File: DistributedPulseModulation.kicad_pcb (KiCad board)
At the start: 2 copper layers, 95.9 x 90.2 mm, 41 parts, among them J1 Conn_02x12_Odd_Even, J2 Conn_02x05_Odd_Even, U1 74LS251, U2 74LVC2G74, U25 74LS85, U28 74LS85, U3 ADG333A, U31 74LS85, U4 MCP23017_SP, U5 ADG333A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

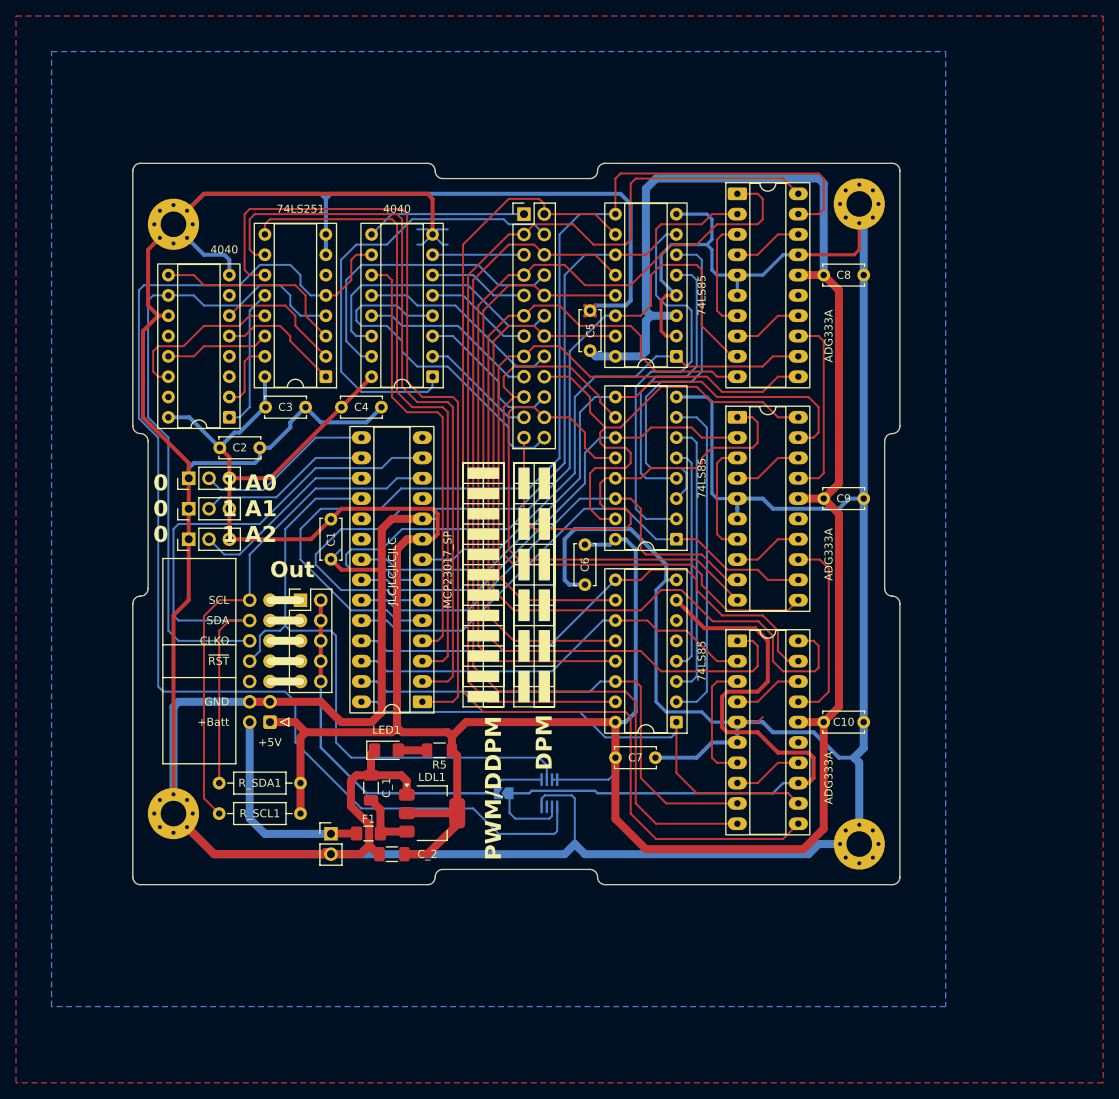
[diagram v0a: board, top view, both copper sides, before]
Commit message: RETROFIT : connecteur perso PCIe_CAN pour compatibilité avec le CANduino128 comme microcontôleur maitre
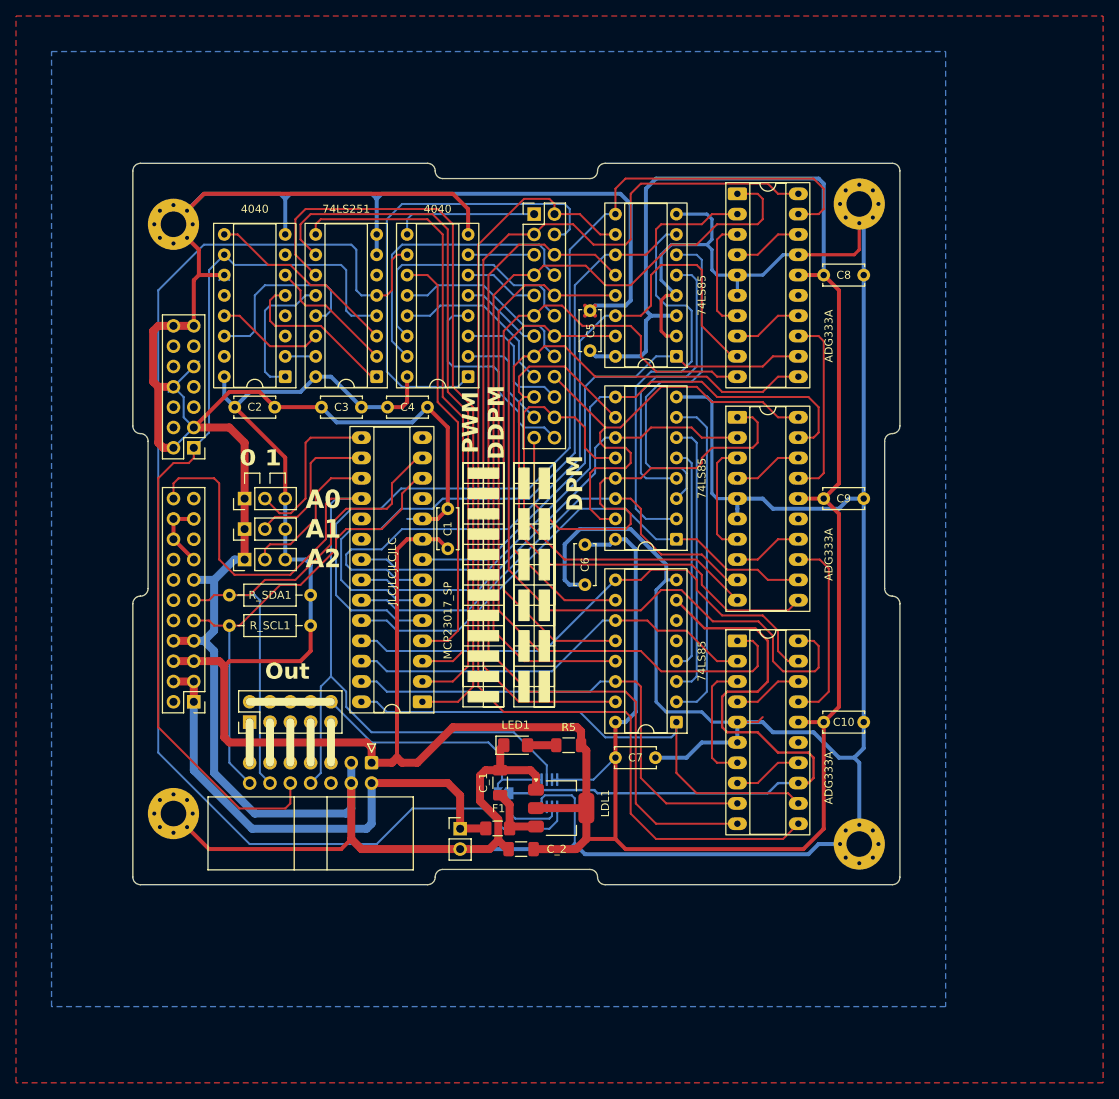
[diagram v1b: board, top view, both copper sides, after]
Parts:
- added PCIe_CAN_1: Conn_02x07_Odd_Even, Connector_PinHeader_2.54mm:PinHeader_2x07_P2.54mm_Vertical, F.Cu at (48.9, 80.0)
- added PCIe_SPI_1: Conn_02x11_Odd_Even, Connector_PinHeader_2.54mm:PinHeader_2x11_P2.54mm_Vertical, F.Cu at (48.9, 111.8)
- moved R_SCL1 23.5 mm to (53.3, 102.2)
- moved R_SDA1 23.5 mm to (53.3, 98.4)
- moved J2 16.5 mm to (55.9, 114.3), turned to 90 degrees
- moved LDL1 16.2 mm to (94.8, 125.0)
- moved R5 16.2 mm to (95.8, 117.2)
- moved C_1 16.2 mm to (87.2, 121.9)
- moved C_2 16.2 mm to (89.8, 130.2)
- moved F1 16.2 mm to (86.9, 127.6)
- moved J_VIN_0 16.2 mm to (82.2, 127.6)
- moved LED1 16.2 mm to (89.1, 117.2)
- moved C1 15.9 mm to (80.6, 87.6), turned to -90 degrees
- moved JP4 13.7 mm to (71.1, 119.4), turned to -90 degrees
- moved U9 8.64 mm to (60.3, 71.1)
- moved JP1 7.43 mm to (55.2, 94.0)
- moved JP2 7.43 mm to (55.2, 90.2)
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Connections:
- U9 pad 12: /Div_512 -> unconnected-(U9-Q8-Pad12)
- U9 pad 15: /Div_2048 -> unconnected-(U9-Q10-Pad15)
- U9 pad 3: /Div_32 -> unconnected-(U9-Q4-Pad3)
- U9 pad 4: /Div_128 -> unconnected-(U9-Q6-Pad4)
- U9 pad 7: /Div_4 -> unconnected-(U9-Q1-Pad7)
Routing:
- net ~{Reset}: track 80.1 -> 117.3 mm
- net VBatt: track 26.2 -> 63.3 mm
- net Clock: track 79.4 -> 111.7 mm
- net Ground: track 763.5 -> 736.0 mm
- net /Q6: track 44.0 -> 26.8 mm
- net +5V: track 423.8 -> 439.1 mm
- net SDA: track 78.8 -> 66.4 mm
- net /A0: track 132.5 -> 122.7 mm
- net /Clock_loc: track 150.5 -> 160.2 mm
- net /Untitled Sheet/+3.3V: track 0.00 -> 8.67 mm
- net /CNT_A4: track 83.0 -> 76.8 mm
- net /CNT_A8: track 83.7 -> 78.0 mm
- net /CNT_A5: track 65.7 -> 60.0 mm
- net Net-(ByPass_2G74-B): track 49.8 -> 44.2 mm
- net /A1: track 101.7 -> 96.0 mm
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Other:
- board text added: "0 1"
- board text added: "A0 A1 A2"
- board text added: "PWM DDPM"
- board text removed: "0 1 A0 0 1 A1 0 1 A2"
- board text removed: "PWM/DDPM"

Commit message: AMELIORATION : simplification des routages de pistes
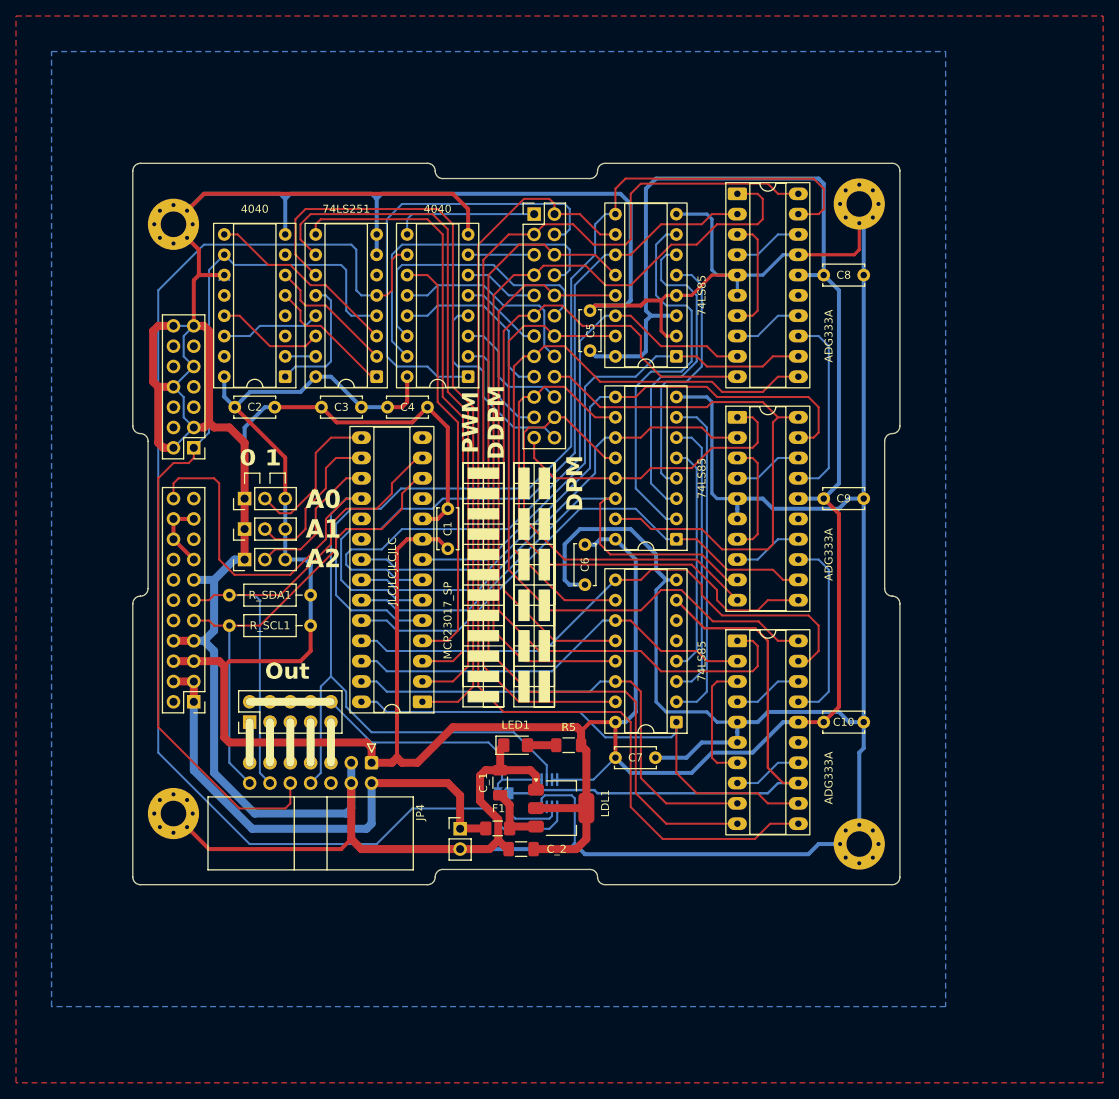
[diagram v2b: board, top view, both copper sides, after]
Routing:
- net +5V: track 439.1 -> 414.6 mm
- net /CNT_A6: track 57.5 -> 38.7 mm
- net Ground: track 736.0 -> 748.9 mm
- net DPM: track 93.0 -> 80.3 mm
- net /CNT_A7: track 58.3 -> 70.8 mm
- net /CNT_A3: track 96.9 -> 85.2 mm
- net /A2: track 95.1 -> 83.5 mm
- net /Div_1024: track 23.5 -> 12.5 mm
- net /CNT_A4: track 76.8 -> 71.0 mm
- net /A8: track 66.3 -> 71.8 mm
- net /A6: track 59.4 -> 64.3 mm
- net /Div_16: track 20.3 -> 15.8 mm
- net /Q10: track 37.0 -> 41.2 mm
- net /CNT_A5: track 60.0 -> 56.0 mm
- net Net-(U25-Oa>b): track 36.8 -> 33.0 mm
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
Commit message: Fin de simplification du routage. Génération des Gerber.
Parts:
- U2: footprint Package_SO_AKL:SSOP-8_2.95x2.8mm_P0.65mm -> Package_SO:SSOP-8_2.95x2.8mm_P0.65mm
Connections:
- net /Untitled Sheet/+3.3V renamed /Bus de fond panier/+3.3V
- net /Untitled Sheet/CAN_0_H renamed /Bus de fond panier/CAN_0_H
- net /Untitled Sheet/CAN_0_L renamed /Bus de fond panier/CAN_0_L
- net /Untitled Sheet/ModBus_A renamed /Bus de fond panier/ModBus_A
- net /Untitled Sheet/ModBus_B renamed /Bus de fond panier/ModBus_B
- net /Untitled Sheet/OSC1 renamed /Bus de fond panier/OSC1
- net /Untitled Sheet/OSC2 renamed /Bus de fond panier/OSC2
- net /Untitled Sheet/SPI_CIPO renamed /Bus de fond panier/SPI_CIPO
- net /Untitled Sheet/SPI_CLK renamed /Bus de fond panier/SPI_CLK
- net /Untitled Sheet/SPI_COPI renamed /Bus de fond panier/SPI_COPI
- net /Untitled Sheet/~{PRSNT1} renamed /Bus de fond panier/~{PRSNT1}
- net /Untitled Sheet/~{PRSNT2} renamed /Bus de fond panier/~{PRSNT2}
- net /Untitled Sheet/~{SPI_CS1} renamed /Bus de fond panier/~{SPI_CS1}
- net /Untitled Sheet/~{SPI_CS2} renamed /Bus de fond panier/~{SPI_CS2}
- net /Untitled Sheet/~{SPI_CS3} renamed /Bus de fond panier/~{SPI_CS3}
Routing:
- net /Clock_loc: track 160.2 -> 106.6 mm
- net +5V: track 414.6 -> 364.9 mm
- net ~{Reset}: track 115.5 -> 150.4 mm
- net Ground: track 748.9 -> 767.1 mm
- net /Q11: track 57.0 -> 42.3 mm
- net /A0: track 122.7 -> 110.4 mm
- net /Div_2: track 24.3 -> 35.0 mm
- net /Q6: track 25.8 -> 32.6 mm
- net /A7: track 65.1 -> 71.5 mm
- net /Div_256: track 13.5 -> 18.8 mm
- net /Q10: track 41.2 -> 35.9 mm
- net /Div_4096: track 16.3 -> 21.5 mm
- net SDA: track 65.6 -> 70.8 mm
- net /A6: track 64.3 -> 69.1 mm
- net /Q9: track 35.0 -> 31.0 mm
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
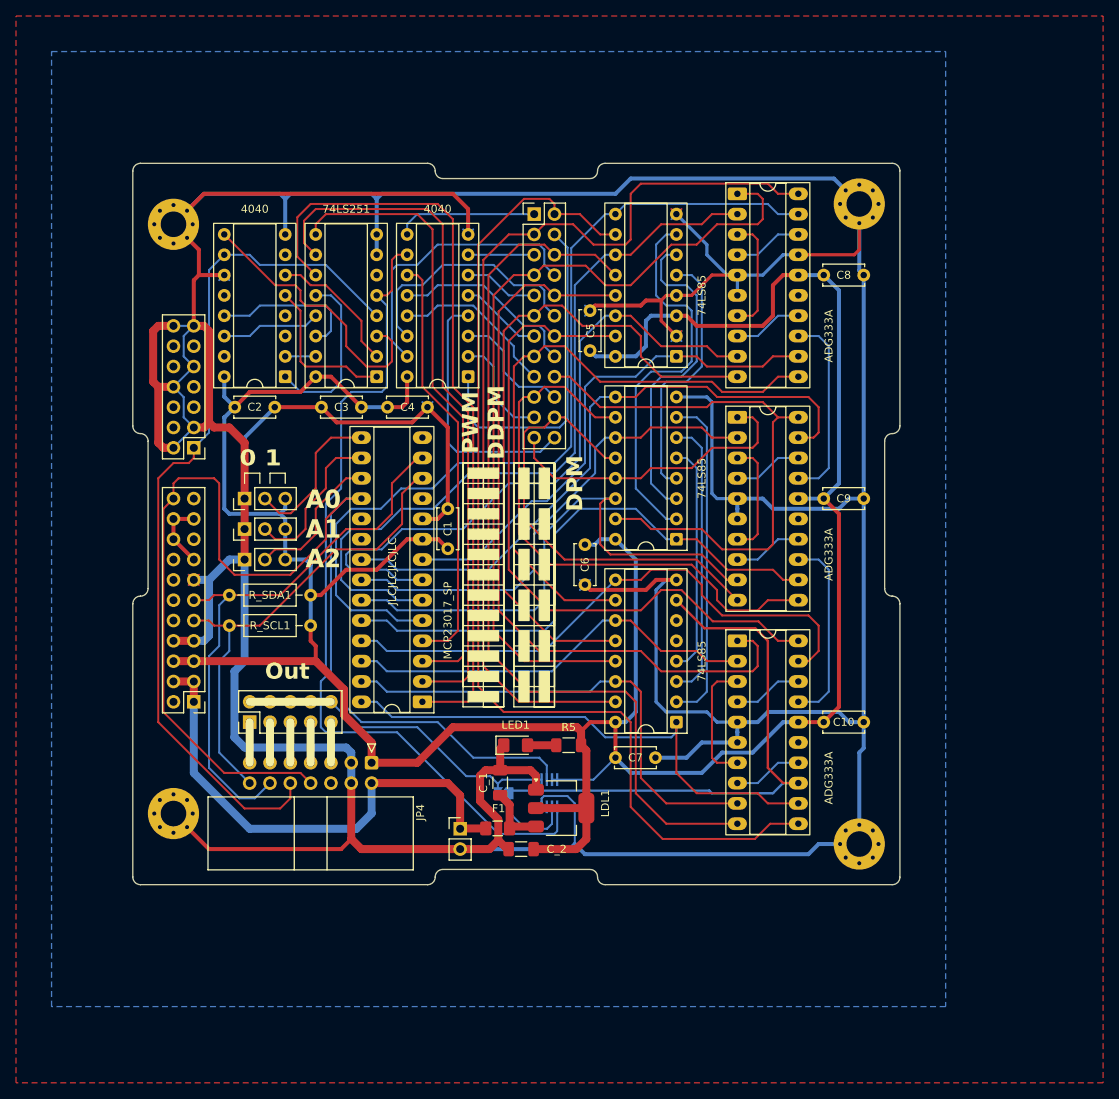
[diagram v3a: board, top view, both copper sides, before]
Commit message: Full rework : ADG333A 10x plus chers que cd74hct4053 Nouveau chips et nouveau routage JPP TT
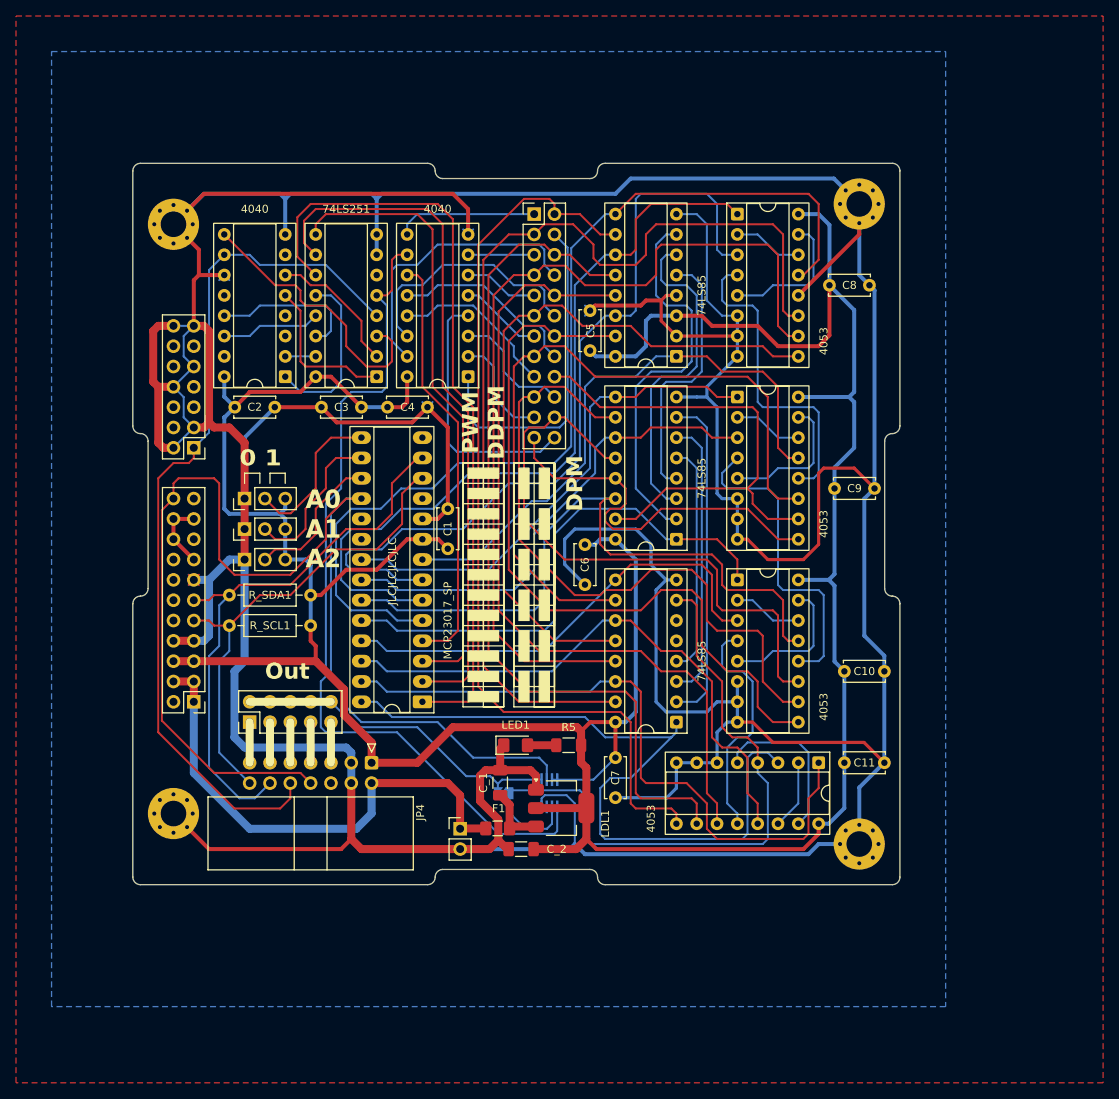
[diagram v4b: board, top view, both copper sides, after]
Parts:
- removed U3, U5, U6: ADG333A, Package_DIP:DIP-20_W7.62mm_Socket_LongPads
- added C11: 0.1µF, Capacitor_THT:C_Disc_D5.0mm_W2.5mm_P5.00mm, F.Cu at (135.2, 119.4)
- added U10: 4053, Package_DIP:DIP-16_W7.62mm_Socket, F.Cu at (116.8, 73.7)
- added U11: 4053, Package_DIP:DIP-16_W7.62mm_Socket, F.Cu at (116.8, 96.5)
- added U12: 4053, Package_DIP:DIP-16_W7.62mm_Socket, F.Cu at (127.0, 119.4)
- added U7: 4053, Package_DIP:DIP-16_W7.62mm_Socket, F.Cu at (116.8, 50.8)
- moved C7 7.07 mm to (101.6, 123.7), turned to 90 degrees
- moved C10 6.85 mm to (135.2, 108.0)
- moved C9 1.85 mm to (134.0, 85.1)
- moved C8 1.46 mm to (133.3, 59.7)
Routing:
- net Ground: track 767.1 -> 812.8 mm
- net Net-(U10-Z): track 0.00 -> 39.8 mm
- net Net-(U10-X0): track 0.00 -> 39.7 mm
- net +5V: track 364.9 -> 404.0 mm
- net Net-(U11-Z): track 0.00 -> 29.7 mm
- net /A11: track 65.9 -> 93.0 mm
- net Net-(U5-D3): track 23.9 -> 0.00 mm
- net Net-(U3-D3): track 23.9 -> 0.00 mm
- net /A10: track 60.7 -> 82.9 mm
- net Net-(U12-Y): track 0.00 -> 20.6 mm
- net /A9: track 52.3 -> 71.4 mm
- net /A2: track 83.5 -> 102.4 mm
- net /CNT_A5: track 56.0 -> 74.9 mm
- net Net-(U11-Y): track 0.00 -> 17.6 mm
- net Net-(U7-Y): track 0.00 -> 17.6 mm
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
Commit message: Simplification du routage
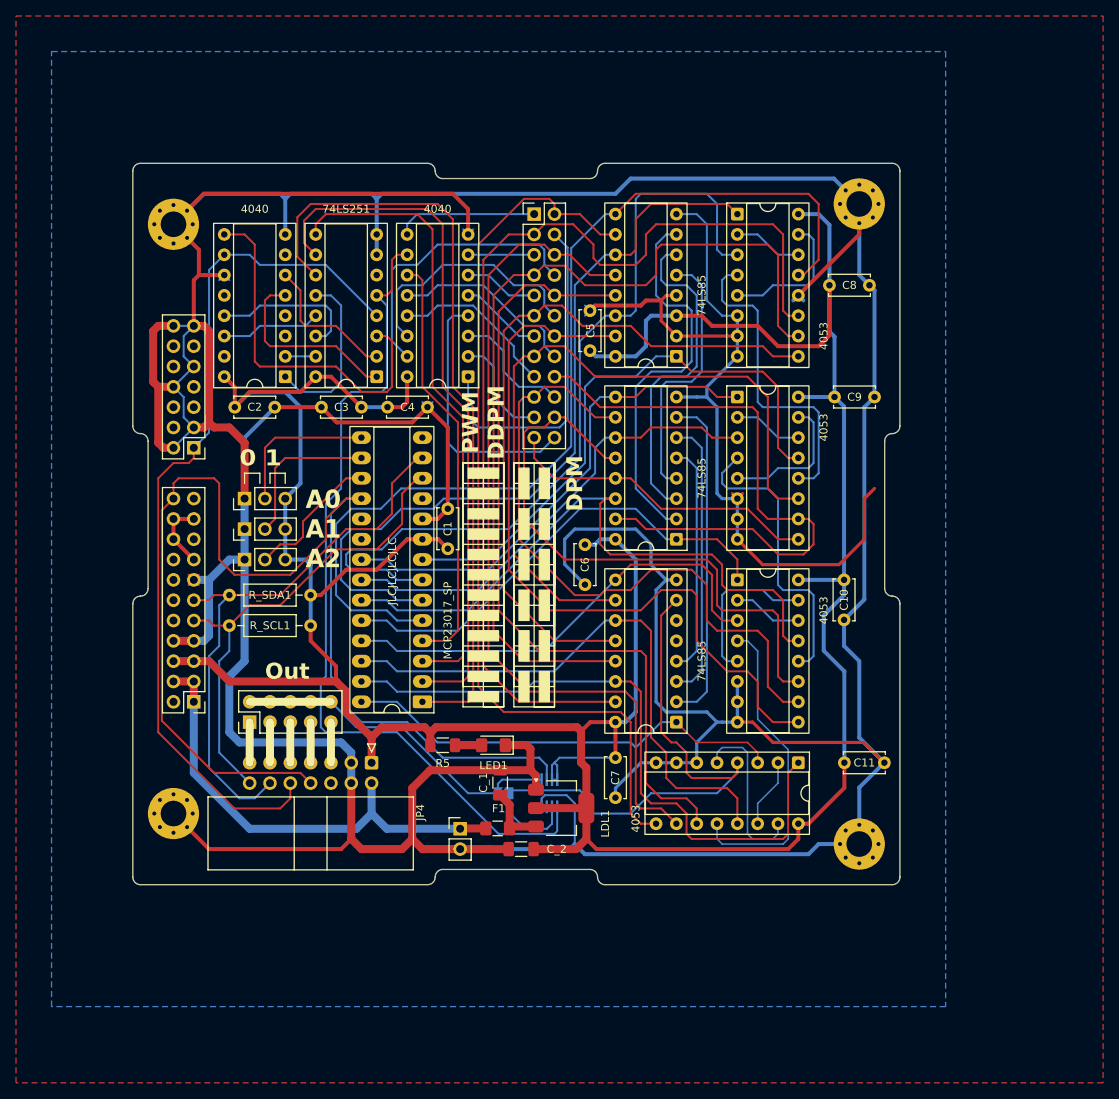
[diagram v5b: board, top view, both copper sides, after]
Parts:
- moved R5 15.7 mm to (80.0, 117.2), turned to 0 degrees
- moved C9 11.4 mm to (134.0, 73.7)
- moved C10 8.17 mm to (130.2, 101.5), turned to 90 degrees
- moved LED1 2.76 mm to (86.4, 117.2), turned to 180 degrees
- moved U12 2.54 mm to (124.5, 119.4)
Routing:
- net /A11: track 93.0 -> 56.1 mm
- net /CNT_A7: track 64.1 -> 76.8 mm
- net /Div_2: track 35.0 -> 45.8 mm
- net Net-(U11-Z): track 29.7 -> 39.5 mm
- net DPM: track 86.9 -> 77.8 mm
- net /CNT_A6: track 48.6 -> 39.8 mm
- net Ground: track 812.8 -> 820.0 mm
- net +5V: track 404.0 -> 411.1 mm
- net /A7: track 65.3 -> 59.0 mm
- net /A6: track 84.0 -> 79.2 mm
- net /Div_16: track 19.4 -> 23.7 mm
- net VBatt: track 62.8 -> 58.8 mm
- net /CNT_A1: track 109.2 -> 105.9 mm
- net /A5: track 60.9 -> 58.3 mm
- net Net-(U10-Z): track 39.8 -> 37.3 mm
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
